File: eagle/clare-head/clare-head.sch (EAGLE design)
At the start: 21 parts

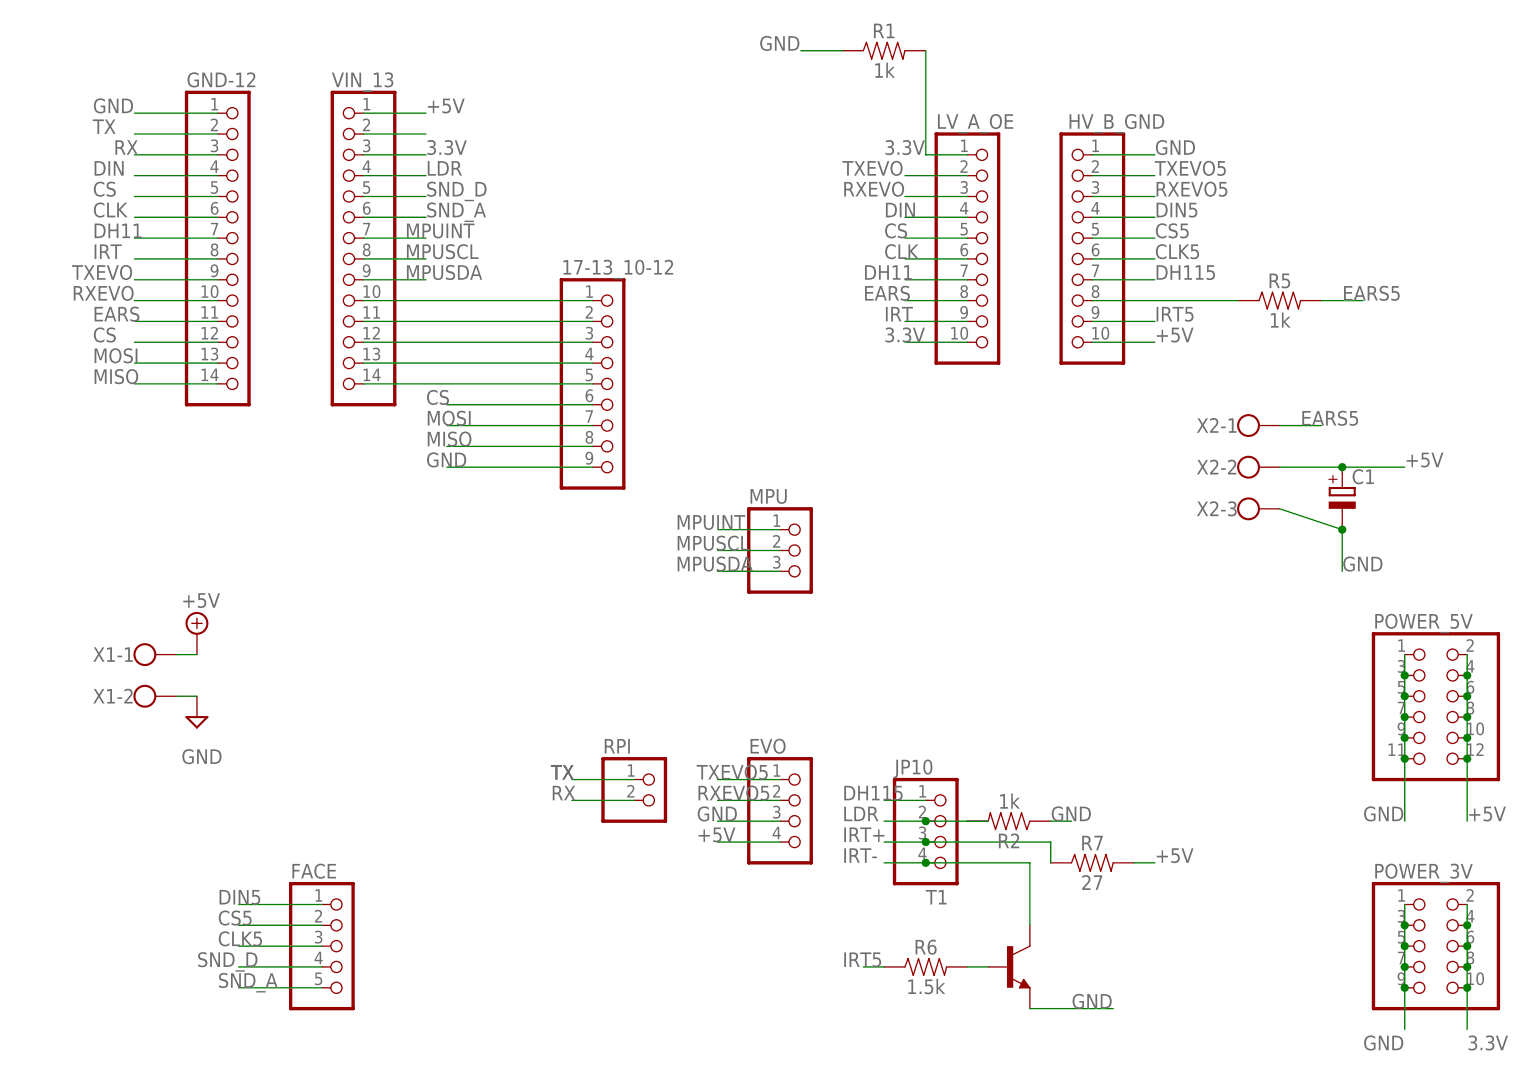
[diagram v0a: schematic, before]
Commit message: Head pcb v2 submitted for manufacture
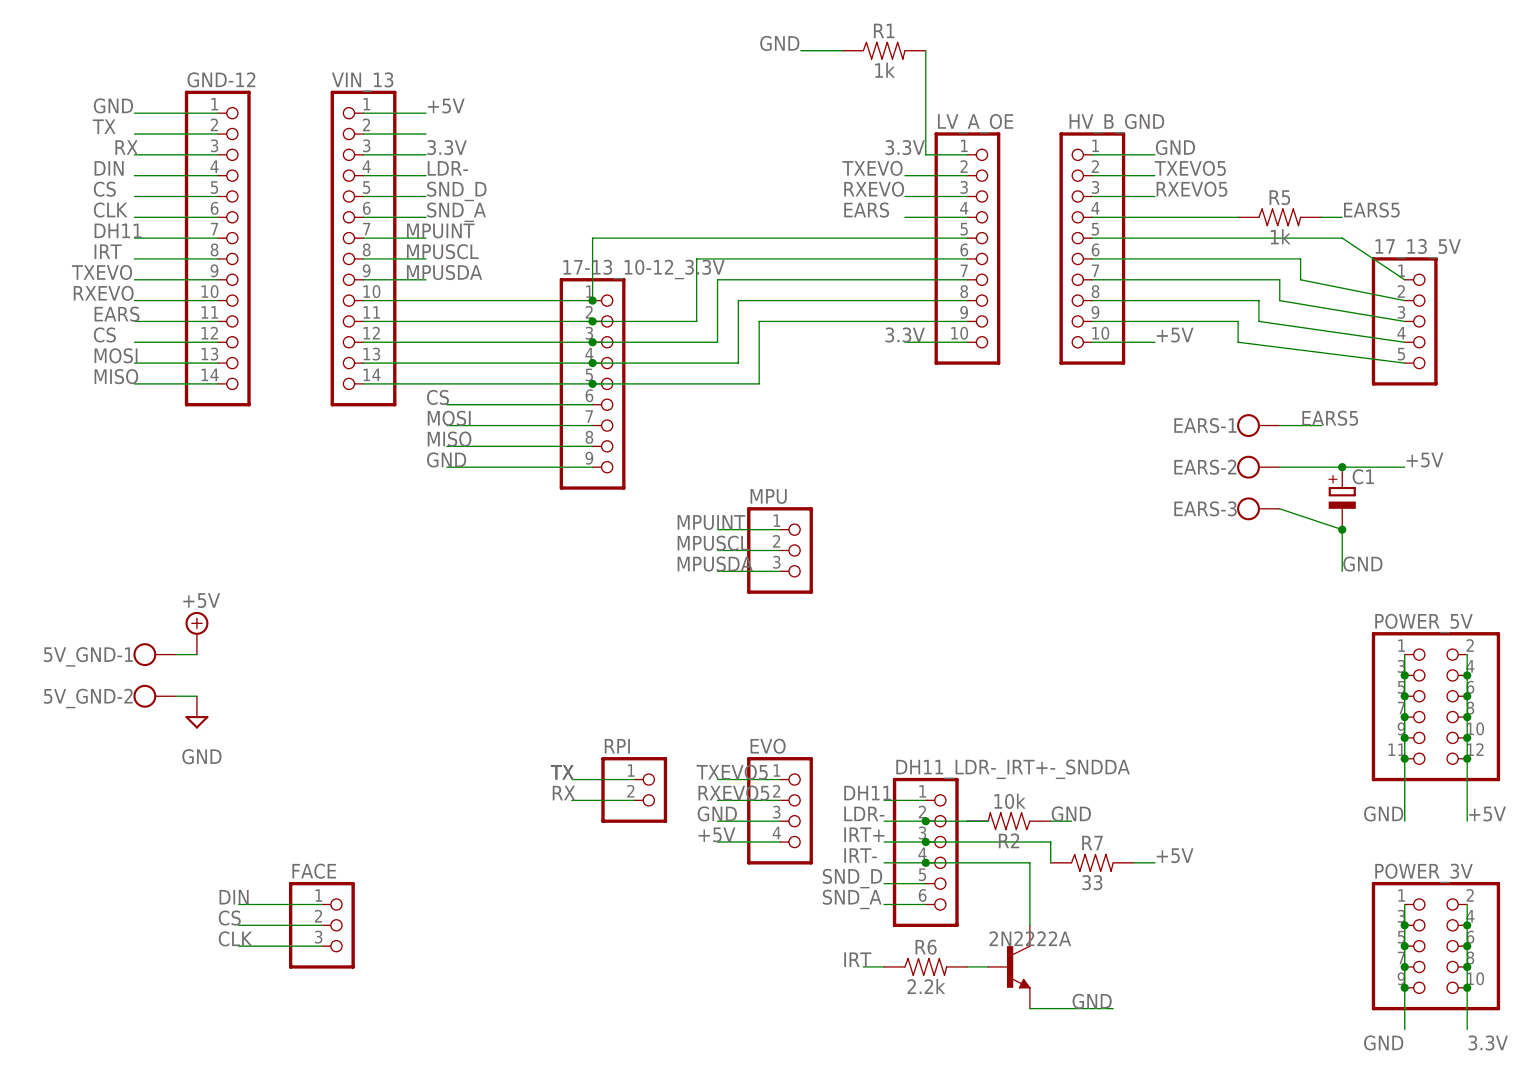
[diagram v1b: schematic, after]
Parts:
- removed JP10: (no value), pinhead:PINHD-1X4
- added 17_13_5V: (no value), pinhead:PINHD-1X5
- added DH11_LDR-_IRT+-_SNDDA: (no value), pinhead:PINHD-1X6
- FACE: device pinhead:PINHD-1X5 -> pinhead:PINHD-1X3
- R2: value 1k -> 10k
- R6: value 1.5k -> 2.2k
- R7: value 27 -> 33
- renumbered 17-13_10-12 to 17-13_10-12_3.3V, T1 to 2N2222A, X1 to 5V_GND, X2 to EARS
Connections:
- removed net CLK5: FACE.3, HV_B_GND.6
- removed net CS5: FACE.2, HV_B_GND.5
- removed net DH115: HV_B_GND.7, JP10.1
- removed net DIN5: FACE.1, HV_B_GND.4
- removed net IRT5: HV_B_GND.9, R6.1
- removed net LDR: JP10.2, R2.2, VIN_13.4
- new net LDR-: DH11_LDR-_IRT+-_SNDDA.2, R2.2, VIN_13.4
- new net N$10: 17_13_5V.5, HV_B_GND.9
- new net N$5: 17_13_5V.1, HV_B_GND.5
- new net N$6: 17_13_5V.2, HV_B_GND.6
- new net N$7: 17_13_5V.3, HV_B_GND.7
- new net N$9: 17_13_5V.4, HV_B_GND.8
- net CLK: now also FACE.3; no longer LV_A_OE.6
- net CS: now also FACE.2; no longer LV_A_OE.5
- net DH11: now also DH11_LDR-_IRT+-_SNDDA.1; no longer LV_A_OE.7
- net DIN: now also FACE.1; no longer LV_A_OE.4
- net EARS: now also LV_A_OE.4; no longer LV_A_OE.8
- net IRT: now also R6.1; no longer LV_A_OE.9
- net IRT+: now also DH11_LDR-_IRT+-_SNDDA.3; no longer JP10.3
- net IRT-: now also DH11_LDR-_IRT+-_SNDDA.4; no longer JP10.4
- net N$12: now also LV_A_OE.5
- net N$13: now also LV_A_OE.6
- net N$14: now also LV_A_OE.7
- net N$15: now also LV_A_OE.8
- net N$16: now also LV_A_OE.9
- net N$8: now also HV_B_GND.4; no longer HV_B_GND.8
- net SND_A: now also DH11_LDR-_IRT+-_SNDDA.6; no longer FACE.5
- net SND_D: now also DH11_LDR-_IRT+-_SNDDA.5; no longer FACE.4
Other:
- moved on the sheet: R5

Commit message: 3d pcb version
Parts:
- removed 17-13_10-12_3.3V: (no value), pinhead:PINHD-1X9
- removed 17_13_5V: (no value), pinhead:PINHD-1X5
- removed DH11_LDR-_IRT+-_SNDDA: (no value), pinhead:PINHD-1X6
- removed RPI: (no value), pinhead:PINHD-1X2
- added 15-13-5V: (no value), pinhead:PINHD-1X3
- added 15-13_10-12_3V: (no value), pinhead:PINHD-1X6
- added DH11_LDR+-_IRT+-_SNDDA: (no value), pinhead:PINHD-1X7
- added RPI-SWPED, SER4: (no value), pinhead:PINHD-1X2
- FACE, MPU: device pinhead:PINHD-1X3 -> pinhead:PINHD-1X5
- POWER_5V: device pinhead:PINHD-2X6 -> pinhead:PINHD-2X4
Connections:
- removed net N$12: 17-13_10-12_3.3V.1, LV_A_OE.5, VIN_13.10
- removed net N$13: 17-13_10-12_3.3V.2, LV_A_OE.6, VIN_13.11
- removed net N$5: 17_13_5V.1, HV_B_GND.5
- removed net N$6: 17_13_5V.2, HV_B_GND.6
- removed net RXEVO5: EVO.2, HV_B_GND.3
- removed net TXEVO5: EVO.1, HV_B_GND.2
- new net 5V: MPU.5
- new net FCS: FACE.2, GND-12.5
- new net RX4: SER4.2, VIN_13.11
- new net TX4: SER4.1, VIN_13.10
- net +5V: no longer POWER_5V.10, POWER_5V.12
- net 3.3V: now also DH11_LDR+-_IRT+-_SNDDA.2, FACE.5
- net CS: now also 15-13_10-12_3V.4; no longer 17-13_10-12_3.3V.6, FACE.2, GND-12.5
- net DH11: now also DH11_LDR+-_IRT+-_SNDDA.1; no longer DH11_LDR-_IRT+-_SNDDA.1
- net GND: now also FACE.4, MPU.4; no longer 17-13_10-12_3.3V.9, POWER_5V.11, POWER_5V.9
- net IRT+: now also DH11_LDR+-_IRT+-_SNDDA.4; no longer DH11_LDR-_IRT+-_SNDDA.3
- net IRT-: now also DH11_LDR+-_IRT+-_SNDDA.5; no longer DH11_LDR-_IRT+-_SNDDA.4
- net LDR-: now also DH11_LDR+-_IRT+-_SNDDA.3; no longer DH11_LDR-_IRT+-_SNDDA.2
- net MISO: now also 15-13_10-12_3V.6; no longer 17-13_10-12_3.3V.8
- net MOSI: now also 15-13_10-12_3V.5; no longer 17-13_10-12_3.3V.7
- net MPUSCL: now also MPU.3; no longer MPU.2
- net MPUSDA: now also MPU.2; no longer MPU.3
- net N$10: now also 15-13-5V.3; no longer 17_13_5V.5
- net N$14: now also 15-13_10-12_3V.1; no longer 17-13_10-12_3.3V.3
- net N$15: now also 15-13_10-12_3V.2; no longer 17-13_10-12_3.3V.4
- net N$16: now also 15-13_10-12_3V.3; no longer 17-13_10-12_3.3V.5
- net N$7: now also 15-13-5V.1; no longer 17_13_5V.3
- net N$9: now also 15-13-5V.2; no longer 17_13_5V.4
- net RX: now also RPI-SWPED.2; no longer RPI.2
- net RXEVO: now also EVO.2; no longer LV_A_OE.3
- net SND_A: now also DH11_LDR+-_IRT+-_SNDDA.7; no longer DH11_LDR-_IRT+-_SNDDA.6
- net SND_D: now also DH11_LDR+-_IRT+-_SNDDA.6; no longer DH11_LDR-_IRT+-_SNDDA.5
- net TX: now also RPI-SWPED.1; no longer RPI.1
- net TXEVO: now also EVO.1; no longer LV_A_OE.2
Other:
- moved on the sheet: EVO, R2

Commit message: Vcc terminal of the imu was not connected, fixed to connect to 3.3
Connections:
- removed net 5V: MPU.5
- net 3.3V: now also MPU.5
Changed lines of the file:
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@@
 <label x="55.88" y="0" size="1.778" layer="95"/>
+</segment>
+<segment>
+<pinref part="MPU" gate="A" pin="5"/>
+<wire x1="53.34" y1="22.86" x2="40.64" y2="22.86" width="0.1524" layer="91"/>
+<label x="38.1" y="22.86" size="1.778" layer="95"/>
 </segment>
 </net>
@@
 </segment>
 </net>
-<net name="5V" class="0">
-<segment>
-<pinref part="MPU" gate="A" pin="5"/>
-<wire x1="53.34" y1="22.86" x2="40.64" y2="22.86" width="0.1524" layer="91"/>
-<label x="38.1" y="22.86" size="1.778" layer="95"/>
-</segment>
-</net>
